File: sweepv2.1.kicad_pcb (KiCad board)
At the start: 2 copper layers, 216.9 x 86.9 mm, 52 parts, among them SW10 SW_Push, SW11 SW_Push, SW11_r1 SW_Push, SW12 SW_Push, SW12_r1 SW_Push, SW13_r1 SW_Push, SW14 SW_Push, SW15 SW_Push, SW15_r1 SW_Push, SW16 SW_Push, SW16_r1 SW_Push, SW17 SW_Push, SW17_r1 SW_Push, SW18 SW_Push, SW18_r1 SW_Push, SW2 SW_Push, SW20 SW_Push, SW20_r1 SW_Push, SW21 SW_Push, SW21_r1 SW_Push, SW2_r1 SW_Push, SW3 SW_Push, SW3_r1 SW_Push, SW4 SW_Push, SW4_r1 SW_Push, SW5 SW_Push, SW5_r1 SW_Push, SW6 SW_Push, SW6_r1 SW_Push, SW7_r1 SW_Push, SW8 SW_Push, SW8_r1 SW_Push, SW9 SW_Push, SW9_r1 SW_Push, U1 ProMicro-kbd, U2 ProMicro-kbd

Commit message: layout finishing touches
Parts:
- added G***: LOGO, jannett_footprints:voyager, F.Cu at (80.5, 84.0)
- added G***: LOGO, jannett_footprints:stars, F.Cu at (80.5, 60.5)
- added G***: LOGO, jannett_footprints:stars, F.Cu at (177.5, 62.5)
- added G***: LOGO, jannett_footprints:saturn, F.Cu at (182.0, 86.0)
- added G***: LOGO, jannett_footprints:stars, B.Cu at (81.5, 61.0)
- added G***: LOGO, jannett_footprints:voyager, B.Cu at (180.3, 83.7)
- added G***: LOGO, jannett_footprints:stars, B.Cu at (177.0, 62.5)
- added G***: LOGO, jannett_footprints:saturn, B.Cu at (77.5, 86.0)
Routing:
- net Switch16: track 47.3 -> 39.5 mm
- net Switch17: track 22.0 -> 20.7 mm
- net Switch1: track 131.1 -> 130.2 mm
- net raw: track 25.0 -> 24.3 mm
- net gnd: vias 1 -> 8

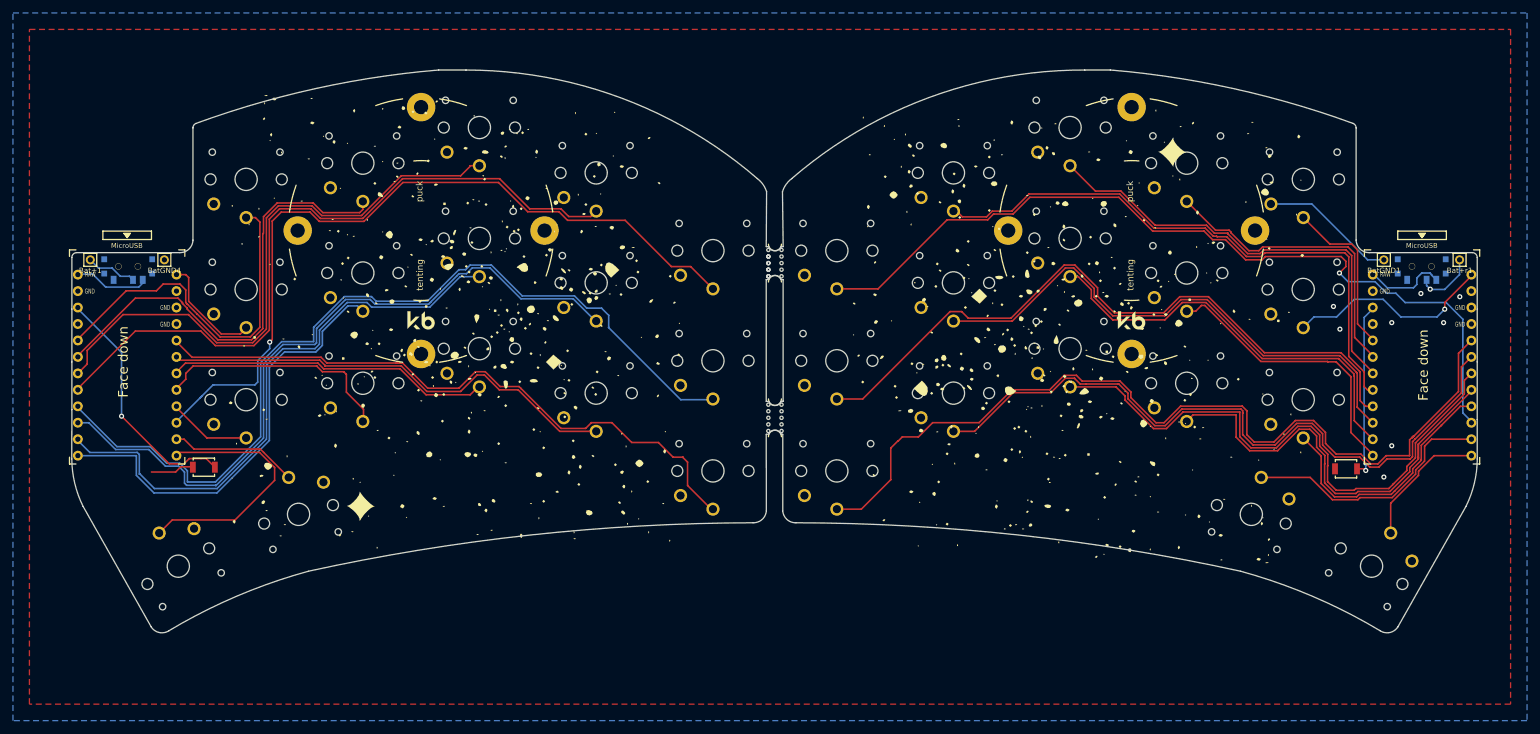
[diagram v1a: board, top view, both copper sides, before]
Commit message: new layout edits for 0305 sockets
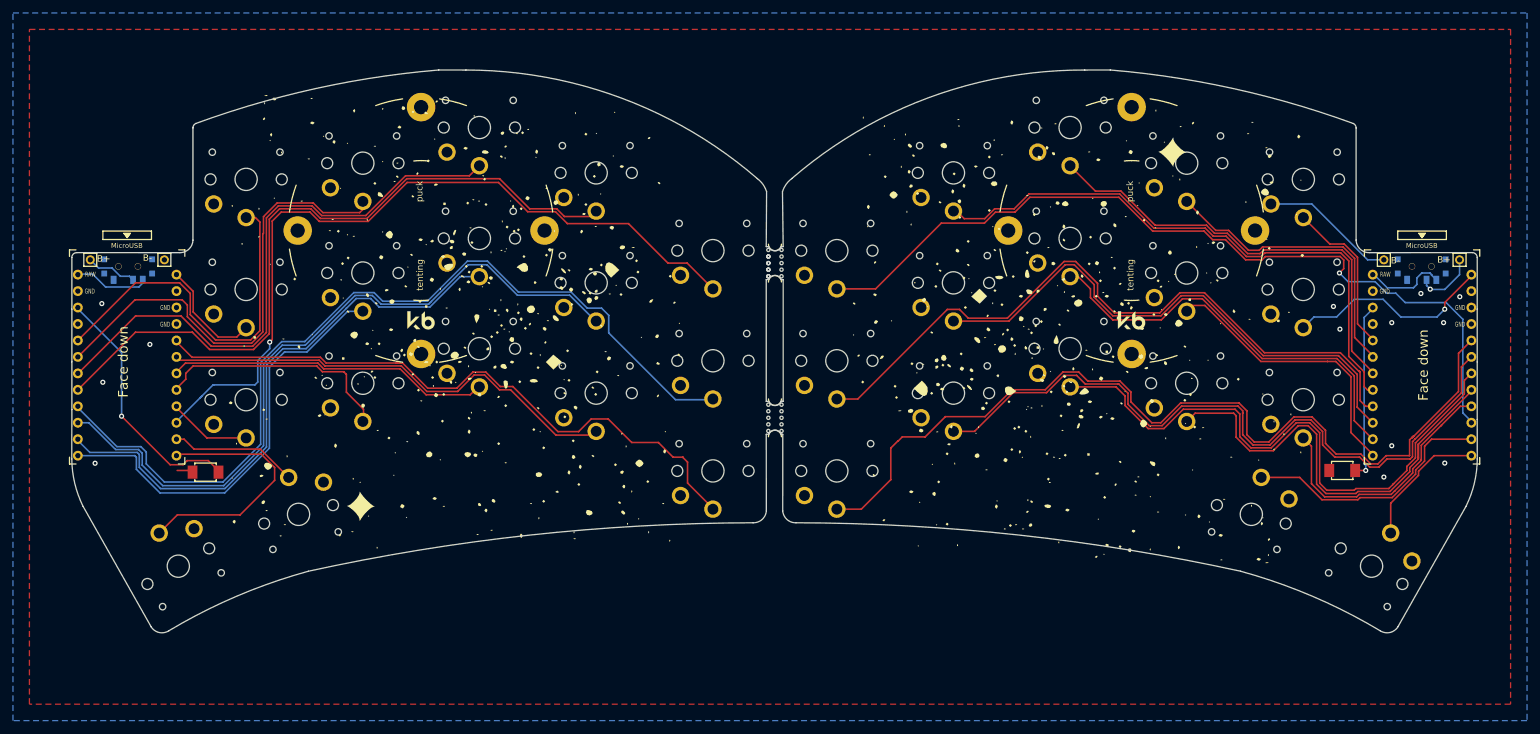
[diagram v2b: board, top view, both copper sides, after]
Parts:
- RSW1, RSW2: footprint kbd:SW_SPST_B3U-1000P -> jannett_footprints:Liyafy_2Pin_SMD_Micro_Switch_3x4x2mm
- SW10, SW11, SW11_r1, SW12, SW12_r1, SW13_r1, SW14, SW15, SW15_r1, SW16, SW16_r1, SW17, SW17_r1, SW18, SW18_r1, SW2, SW20, SW20_r1, SW21, SW21_r1, SW2_r1, SW3, SW3_r1, SW4, SW4_r1, SW5, SW5_r1, SW6, SW6_r1, SW7_r1, SW8, SW8_r1, SW9, SW9_r1: footprint Kailh:SW_PG1350_nonrev_DPB -> jannett_footprints:kailh_low_profile_0305_sockets
- moved RSW2 0.80 mm to (42.4, 83.6)
- moved RSW1 0.64 mm to (217.9, 83.3)
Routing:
- net gnd: track 27.7 -> 23.6 mm, vias 8 -> 13
- net Switch13: track 90.5 -> 92.6 mm
- net Switch9_r: track 68.5 -> 66.6 mm
- net Switch12: track 108.4 -> 110.3 mm
- net Switch11: track 136.7 -> 138.5 mm
- net Switch6: track 106.6 -> 108.2 mm
- net Switch14: track 68.6 -> 70.1 mm
- net Switch5_r: track 55.7 -> 57.1 mm
- net Switch4_r: track 71.6 -> 72.8 mm
- net Switch7: track 83.9 -> 85.1 mm
- net Switch6_r: track 136.2 -> 137.1 mm
- net Switch15: track 40.1 -> 41.0 mm
- net Switch11_r: track 99.8 -> 100.6 mm
- net Switch3_r: track 91.4 -> 90.7 mm
- net Switch5: track 25.5 -> 24.8 mm
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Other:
- board text added: "+"
- board text added: "-"
- board text added: "B+"
- board text added: "B-"
- board text added: "Ferris Cosmic"
- board text added: "ON <-> OFF"
- board text removed: "Sweep v 2.1"
